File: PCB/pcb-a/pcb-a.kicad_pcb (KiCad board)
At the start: 2 copper layers, 109.7 x 43.5 mm, 28 parts, among them Q3 BC337, SW1 config, U1 ESP32-S2-DevKitM

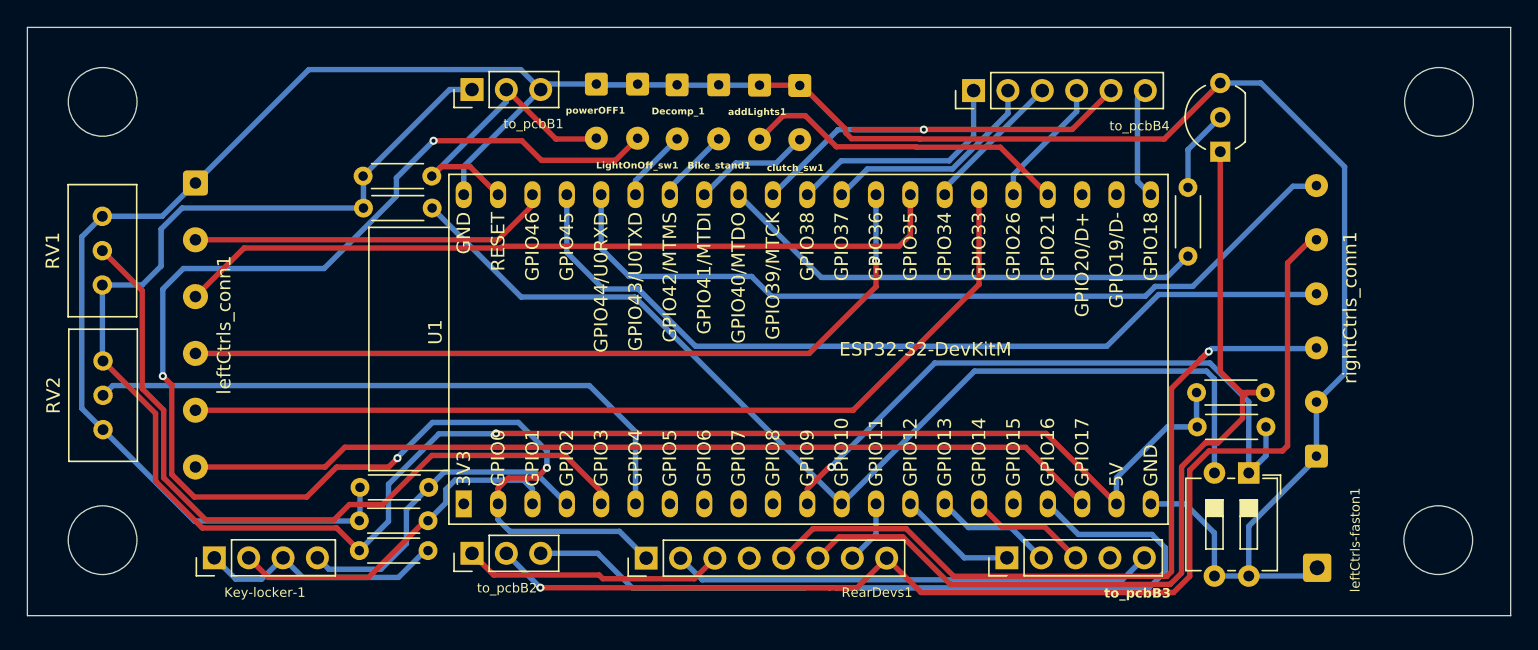
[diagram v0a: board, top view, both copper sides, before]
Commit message: Fixes and updates
This version will be tested soon. It is fully implemented with THT devices using ESP32-S2 DevKit
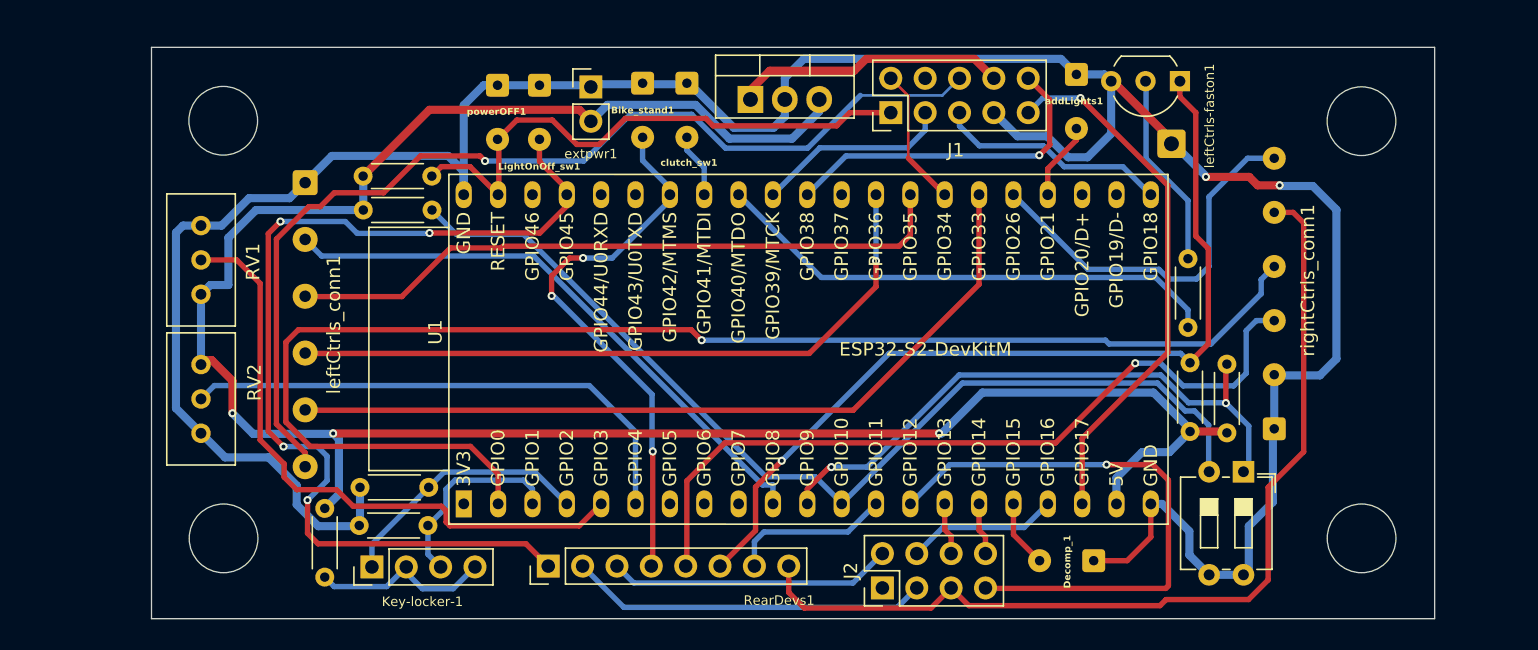
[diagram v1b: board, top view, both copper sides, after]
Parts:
- removed to_pcbB1, to_pcbB2: Conn_01x03, Connector_PinHeader_2.54mm:PinHeader_1x03_P2.54mm_Vertical
- removed to_pcbB3: Conn_01x05, Connector_PinHeader_2.54mm:PinHeader_1x05_P2.54mm_Vertical
- removed to_pcbB4: Conn_01x06, Connector_PinHeader_2.54mm:PinHeader_1x06_P2.54mm_Vertical
- added J1: Conn_02x05_Counter_Clockwise, Connector_PinHeader_2.54mm:PinHeader_2x05_P2.54mm_Vertical, F.Cu at (166.2, 67.0)
- added J2: Conn_02x04_Counter_Clockwise, Connector_PinHeader_2.54mm:PinHeader_2x04_P2.54mm_Vertical, F.Cu at (165.6, 102.1)
- added U3: L7805, Package_TO_SOT_THT:TO-220-3_Vertical, F.Cu at (155.8, 66.0)
- added extpwr1: Conn_01x02, Connector_PinHeader_2.54mm:PinHeader_1x02_P2.54mm_Vertical, F.Cu at (144.0, 65.0)
- moved Decomp_1 46.8 mm to (181.2, 100.1), turned to 180 degrees
- moved leftCtrls-faston1 33.1 mm to (186.9, 69.2)
- moved addLights1 23.4 mm to (179.9, 64.1)
- moved Key-locker-1 11.7 mm to (127.8, 100.5)
- moved clutch_sw1 8.35 mm to (151.1, 64.8)
- moved leftCtrls_conn1 8.11 mm to (122.9, 72.1)
- moved RV1 7.33 mm to (115.2, 75.3)
- moved powerOFF1 7.31 mm to (137.1, 64.9)
- moved RearDevs1 7.26 mm to (140.8, 100.5)
- moved LightOnOff_sw1 7.26 mm to (140.2, 64.9)
- moved RV2 7.25 mm to (115.2, 85.6)
- moved Q3 6.01 mm to (187.6, 64.6), turned to 180 degrees
- moved R6 5.98 mm to (188.3, 85.4), turned to -90 degrees
- moved Bike_stand1 5.63 mm to (147.8, 64.8)
- moved R7 5.27 mm to (188.1, 77.8)
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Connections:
- net tempPower renamed 5V
- Key-locker-1 pad 1: Net-(Key-locker-1-Pin_1) -> i_Vx2
- Key-locker-1 pad 2: i_Vx1 -> Net-(Key-locker-1-Pin_2)
- Key-locker-1 pad 3: Net-(Key-locker-1-Pin_1) -> i_Vx1
- Key-locker-1 pad 4: i_Vx2 -> Net-(Key-locker-1-Pin_2)
- R1 pad 2: Net-(Key-locker-1-Pin_1) -> Net-(Key-locker-1-Pin_2)
- RearDevs1 pad 4: unconnected-(RearDevs1-Pin_4-Pad4) -> i_bykeStand
- U1 pad 10: unconnected-(U1-GPIO8/TOUCH8/ADC1_CH7-Pad10) -> i_leftArrow
- U1 pad 17: unconnected-(U1-GPIO15/U0RTS/ADC2_CH4/XTAL_32K_P-Pad17) -> i_decompr
- U1 pad 19: i_horn -> o_upLight
- U1 pad 2: c_rearLight -> i_startButton
- U1 pad 26: o_horn -> i_engineON
- U1 pad 31: o_upLight -> unconnected-(U1-GPIO37-Pad31)
- U1 pad 37: i_decompr -> unconnected-(U1-U0TXD/GPIO43/CLK_OUT1-Pad37)
- U1 pad 38: i_engineON -> unconnected-(U1-U0RXD/GPIO44/CLK_OUT2-Pad38)
- U1 pad 39: i_startButton -> c_rearLight
- U1 pad 40: i_leftArrow -> unconnected-(U1-GPIO46/LOG-Pad40)
- leftCtrls_conn1 pad 6: i_horn -> c_horn
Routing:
- net c_horn: track 0.00 -> 75.5 mm, vias 0 -> 1
- net i_horn: track 67.9 -> 0.00 mm
- net o_engineON: track 59.5 -> 11.2 mm
- net i_startButton: track 64.2 -> 102.3 mm, vias 0 -> 1
- net i_bykeStand: track 5.62 -> 41.2 mm, vias 0 -> 3
- net o_keepAlive: track 8.79 -> 42.2 mm, vias 0 -> 1
- net i_engineON: track 61.7 -> 28.6 mm
- net c_rearLight: track 107.2 -> 74.2 mm
- net o_upLight: track 16.5 -> 39.6 mm, vias 0 -> 1
- net Net-(J1-Pin_8): track 0.00 -> 20.2 mm
- net i_powerOFF: track 22.9 -> 42.0 mm
- net o_rightArrow: track 33.4 -> 14.5 mm, vias 1 -> 0
- net i_addLight: track 24.5 -> 5.85 mm
- net Net-(Key-locker-1-Pin_1): track 18.5 -> 0.00 mm
- net i_leftArrow: track 26.8 -> 43.5 mm
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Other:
- board size 109.7 x 43.5 mm -> 94.9 x 42.2 mm

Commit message: Changes to reduce PCB size
- The resistors type has been changed from THT to SMD
- Configuration switches has been moved to fit PCB space in better way
- An electrolitic capicitor has been added
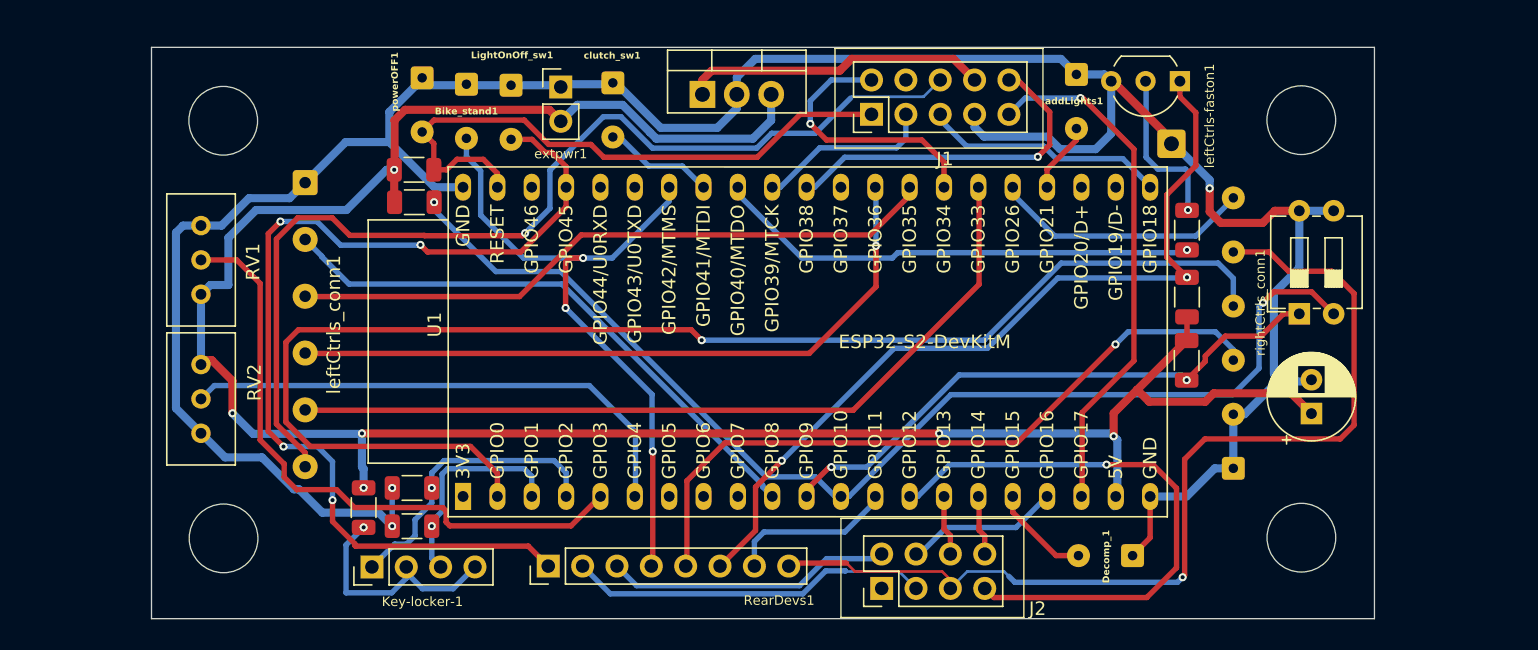
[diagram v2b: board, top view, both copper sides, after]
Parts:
- added C1: 10uF, Capacitor_THT:CP_Radial_D6.3mm_P2.50mm, F.Cu at (197.3, 89.2)
- R1, R2, R3, R4, R5, R6, R7, R8: footprint Resistor_THT:R_Axial_DIN0204_L3.6mm_D1.6mm_P5.08mm_Horizontal -> Resistor_SMD:R_1206_3216Metric
- moved Bike_stand1 13.0 mm to (134.8, 64.8)
- moved SW1 12.4 mm to (196.4, 81.8), turned to 90 degrees
- moved R8 6.13 mm to (188.1, 85.3), turned to -90 degrees
- moved powerOFF1 5.60 mm to (131.5, 64.4)
- moved clutch_sw1 5.48 mm to (145.6, 64.8)
- moved R6 4.86 mm to (188.1, 80.6)
- moved rightCtrls_conn1 4.21 mm to (191.5, 93.2)
- moved R3 3.90 mm to (130.8, 97.5)
- moved R4 3.84 mm to (130.8, 94.7)
- moved R5 3.82 mm to (130.9, 73.6)
- moved U3 3.57 mm to (152.2, 65.6)
- moved Decomp_1 2.90 mm to (184.1, 99.7)
- moved R1 2.88 mm to (127.2, 96.2)
- moved extpwr1 2.22 mm to (141.8, 65.0)
- moved R7 2.11 mm to (188.1, 75.6)
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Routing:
- net Net-(U1-GPIO10/TOUCH10/ADC1_CH9/FSPICS0/FSPIIO4): track 74.9 -> 85.4 mm, vias 0 -> 2
- net i_bykeStand: track 41.2 -> 50.8 mm
- net i_engineON: track 28.6 -> 19.3 mm
- net 5V: track 161.1 -> 170.0 mm, vias 3 -> 6
- net o_addLight: track 11.4 -> 19.9 mm, vias 0 -> 1
- net GND: track 206.5 -> 198.4 mm, vias 2 -> 3
- net c_brakeSwitch: track 57.9 -> 52.6 mm
- net Net-(Key-locker-1-Pin_2): track 13.6 -> 17.8 mm, vias 0 -> 1
- net i_powerOFF: track 42.0 -> 46.2 mm
- net c_engineOFF: track 69.8 -> 73.7 mm, vias 0 -> 1
- net c_startEngine: track 65.7 -> 62.1 mm, vias 1 -> 2
- net i_clutch: track 4.77 -> 8.24 mm
- net i_Vx2: track 19.5 -> 22.0 mm, vias 0 -> 1
- net Net-(Q3-B): track 14.4 -> 12.0 mm, vias 0 -> 1
- net Net-(U1-GPIO9/TOUCH9/ADC1_CH8/FSPIHD): track 45.4 -> 43.0 mm
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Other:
- board size 94.9 x 42.2 mm -> 90.4 x 42.2 mm

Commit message: Small changes for PCB size reducing
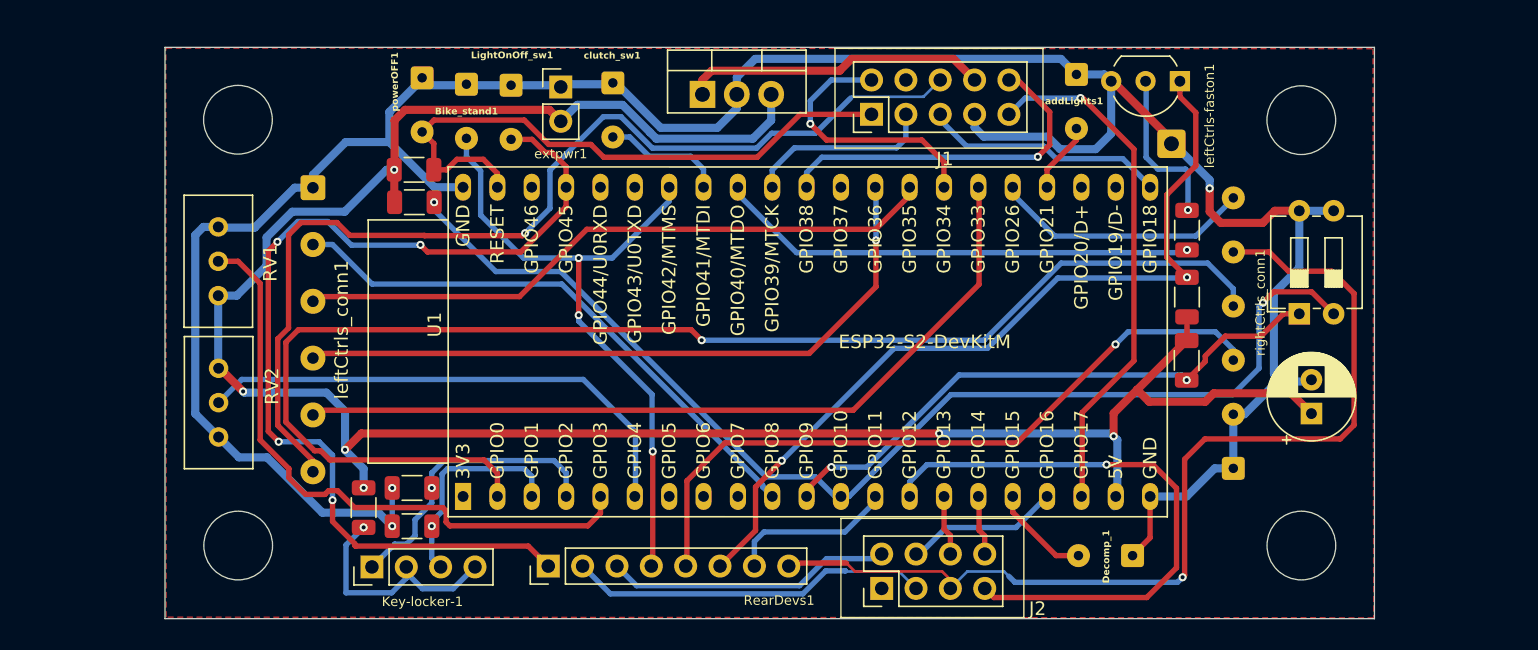
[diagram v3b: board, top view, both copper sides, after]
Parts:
- moved RV2 1.33 mm to (116.5, 85.8)
- moved RV1 1.28 mm to (116.5, 75.4)
- moved leftCtrls_conn1 0.69 mm to (123.5, 72.5)
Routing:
- net 5V: track 170.0 -> 167.0 mm
- net GND: track 198.4 -> 196.3 mm
- net i_bykeStand: track 50.8 -> 49.3 mm
- net Net-(U1-GPIO4/TOUCH4/ADC1_CH3): track 38.8 -> 37.9 mm
- net i_clutch: track 8.24 -> 9.02 mm
- net i_leftArrow: track 42.5 -> 41.8 mm
- net o_rightArrow: track 13.2 -> 13.9 mm
- net o_downLight: track 25.7 -> 26.3 mm
- net o_keepAlive: track 42.7 -> 43.3 mm
- net Net-(U1-GPIO3/TOUCH3/ADC1_CH2): track 46.9 -> 46.4 mm
- added copper zone on F.Cu, net GND
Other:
- board size 90.4 x 42.2 mm -> 89.4 x 42.2 mm

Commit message: Fixes
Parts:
- removed Bike_stand1: Conn_01x02, Connector_Wire:SolderWire-0.15sqmm_1x02_P4mm_D0.5mm_OD1.5mm
- Decomp_1, LightOnOff_sw1, addLights1, clutch_sw1, powerOFF1: footprint Connector_Wire:SolderWire-0.15sqmm_1x02_P4mm_D0.5mm_OD1.5mm -> Connector_Wire:SolderWire-0.75sqmm_1x02_P4.8mm_D1.25mm_OD2.3mm
- J2: value Conn_02x04_Counter_Clockwise -> Conn_02x05_Counter_Clockwise; footprint Connector_PinHeader_2.54mm:PinHeader_2x04_P2.54mm_Vertical -> Connector_PinHeader_2.54mm:PinHeader_2x05_P2.54mm_Vertical
- extpwr1: footprint Connector_PinHeader_2.54mm:PinHeader_1x02_P2.54mm_Vertical -> Connector_Wire:SolderWire-0.75sqmm_1x02_P4.8mm_D1.25mm_OD2.3mm
- rightCtrls_conn1: footprint Connector_Wire:SolderWire-0.15sqmm_1x06_P4mm_D0.5mm_OD1.5mm -> Connector_Wire:SolderWire-0.25sqmm_1x06_P4.2mm_D0.65mm_OD1.7mm
- moved R4 12.0 mm to (142.1, 90.7), turned to -90 degrees
- moved R3 11.1 mm to (139.4, 90.6), turned to -90 degrees
- moved LightOnOff_sw1 6.62 mm to (131.5, 64.4)
- moved extpwr1 5.83 mm to (136.0, 64.3), turned to -90 degrees
- moved clutch_sw1 5.15 mm to (140.5, 64.3)
- moved R5 5.14 mm to (134.9, 76.8), turned to -90 degrees
- moved R8 4.52 mm to (185.1, 88.7)
- moved powerOFF1 4.42 mm to (127.1, 64.3)
- moved R1 4.38 mm to (131.6, 96.1)
- moved R6 4.10 mm to (185.1, 83.4)
- moved R7 3.81 mm to (185.1, 78.0)
- moved rightCtrls_conn1 2.67 mm to (189.2, 94.6)
- moved Q3 2.45 mm to (190.0, 64.6)
- moved R2 2.30 mm to (130.1, 73.3)
- moved U3 2.18 mm to (150.1, 65.5)
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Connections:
- J2 pad 5: c_engineOFF -> unconnected-(J2-Pin_5-Pad5)
- J2 pad 6: o_engineReady -> unconnected-(J2-Pin_6-Pad6)
- J2 pad 7: o_keepAlive -> c_engineOFF
- J2 pad 8: o_neutral -> o_engineReady
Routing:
- net o_keepAlive: track 43.3 -> 17.7 mm
- net i_bykeStand: track 49.3 -> 33.7 mm
- net i_decompr: track 7.35 -> 21.5 mm, vias 0 -> 1
- net GND: track 196.3 -> 208.1 mm, vias 3 -> 1
- net Net-(U1-GPIO10/TOUCH10/ADC1_CH9/FSPICS0/FSPIIO4): track 85.4 -> 75.6 mm, vias 2 -> 1
- net i_startButton: track 100.0 -> 91.0 mm
- net Net-(Key-locker-1-Pin_2): track 17.8 -> 11.2 mm
- net o_leftArrow: track 18.0 -> 23.5 mm
- net o_upLight: track 38.6 -> 43.7 mm
- net i_clutch: track 9.02 -> 14.0 mm
- net c_rearLight: track 74.2 -> 78.9 mm
- net c_startEngine: track 62.1 -> 66.0 mm
- net c_brakeSwitch: track 52.6 -> 48.8 mm
- net i_Vx2: track 22.0 -> 25.6 mm, vias 1 -> 0
- net o_startEngine: track 36.2 -> 33.1 mm
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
